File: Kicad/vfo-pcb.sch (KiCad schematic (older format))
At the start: 83 parts, among them J1 Rotery Encoder1, J10 Link-out 1-2, J11 Link-out 1-0, J12 Link-out 2-0, J13 Link-out 2-2, J14 Link-out 2-1, J15 Link-out 1-1, J2 Rotery Encoder2, J3 Analog in 3-6, J4 RxTx, J5 V12, J6 ESP32L, J7 ESP32R, J8 ILI9341, J9 Conn_01x07_Female, Q1 BFR92, Q2 BFR92, Q3 BFR92, Q4 BFR92, Q5 BFR92, Q6 BFR92, SW1 Rotary_Encoder_Switch, U1 AMS1117, U2 L7805, U3 Si5351A-B-GT, U4 Si5351A-B-GT, Y1 Crystal, Y2 Crystal

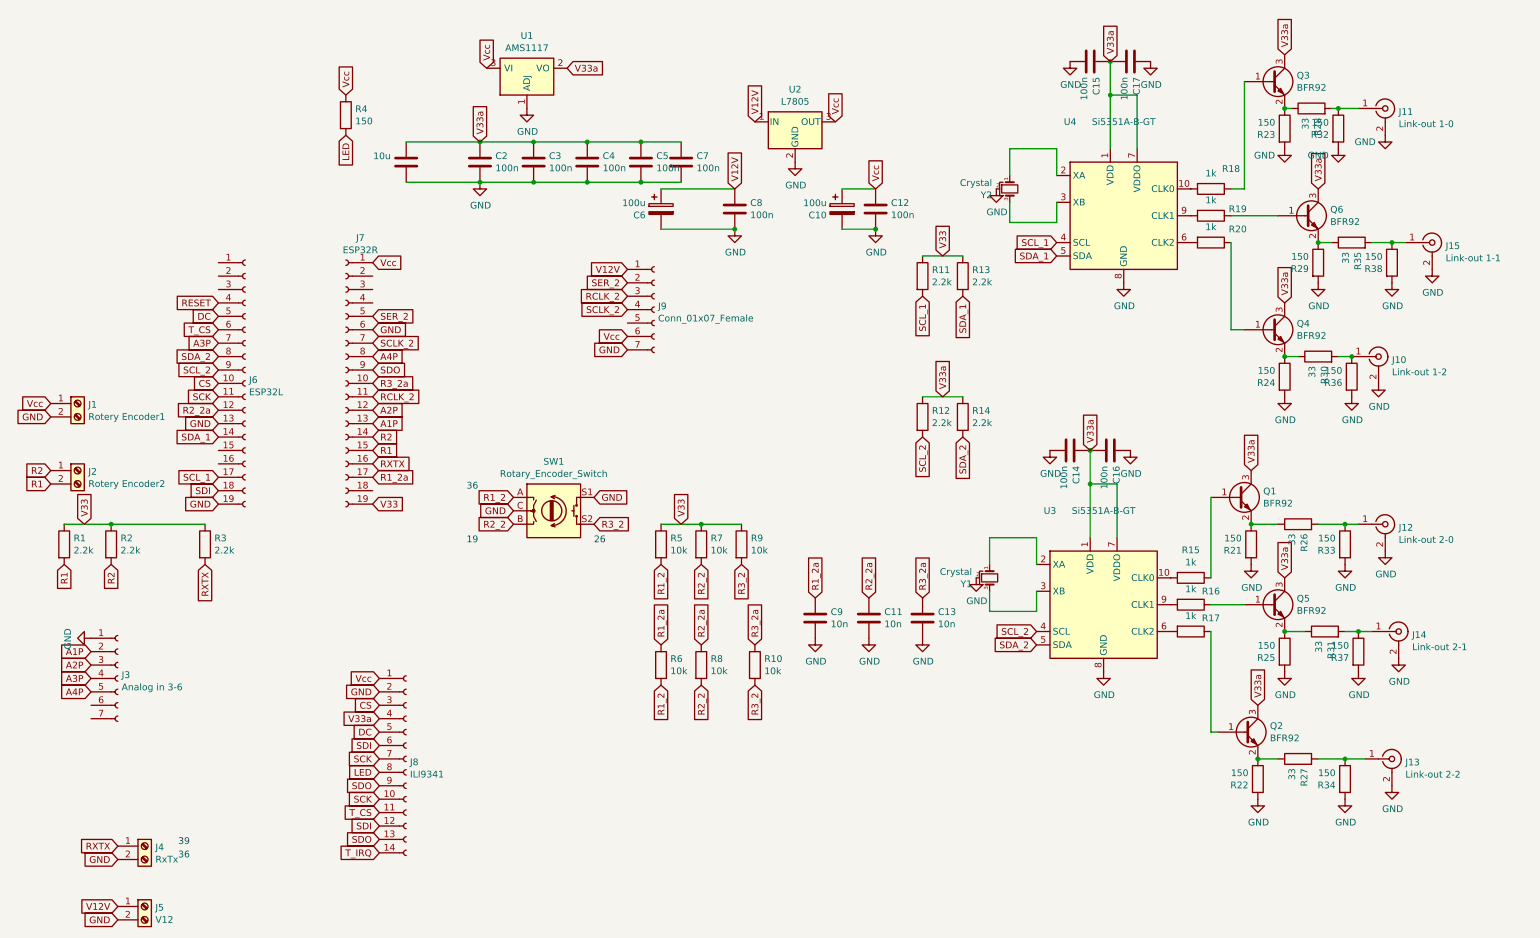
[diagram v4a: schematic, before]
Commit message: wifi update LM7805 version
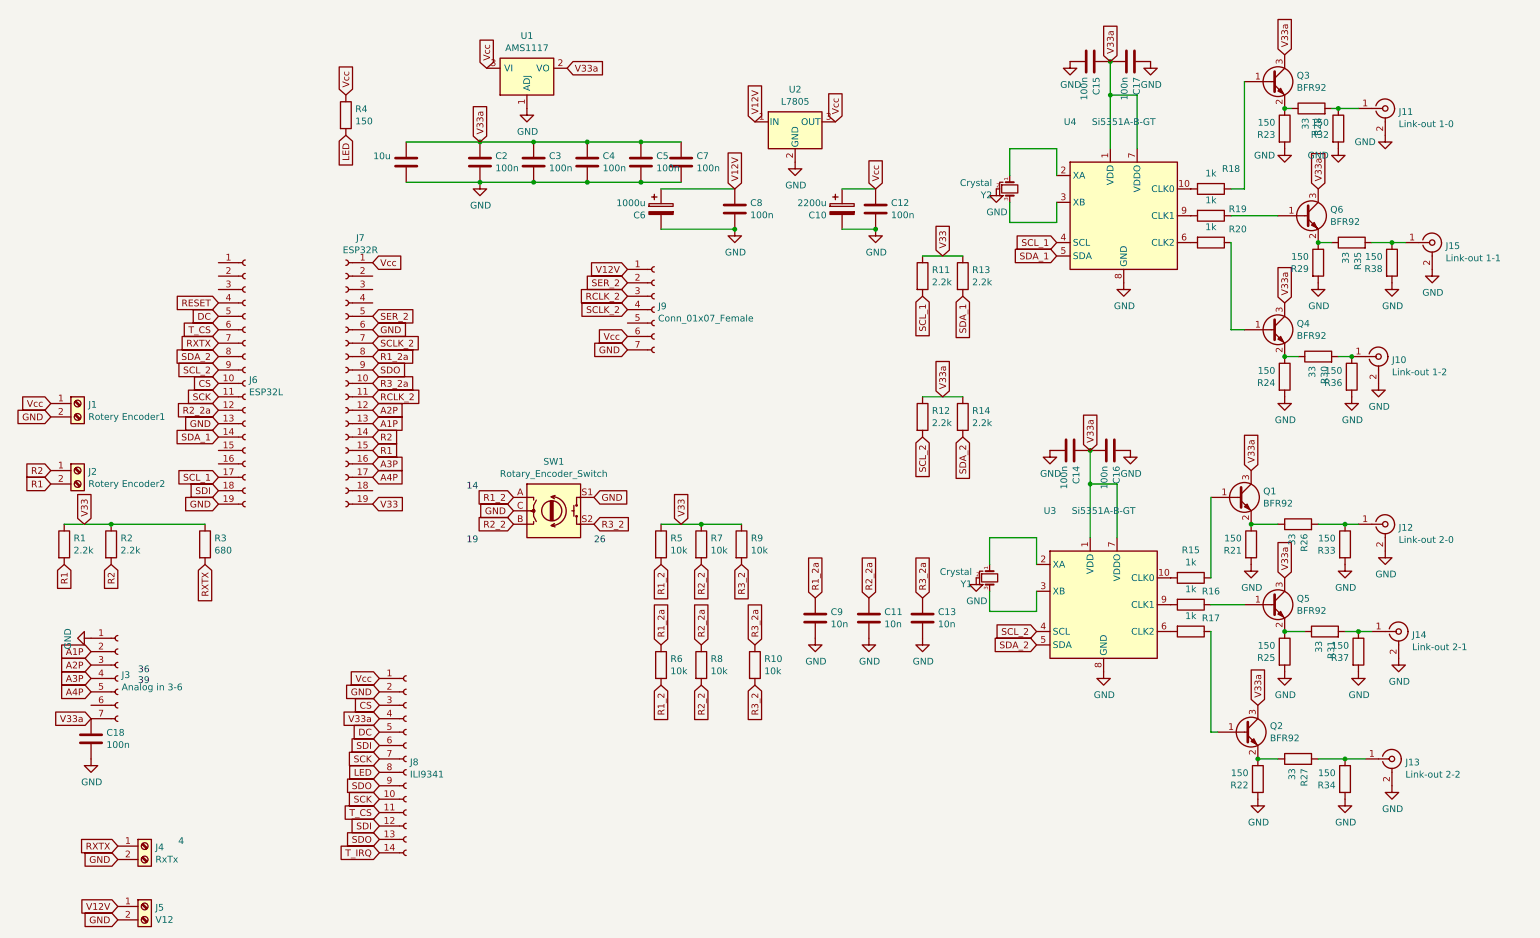
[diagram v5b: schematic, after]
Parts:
- added C18: 100n, Capacitor_SMD:C_1206_3216Metric_Pad1.42x1.75mm_HandSolder, symbol Device:C
- C10: value 100u -> 2200u; footprint Capacitor_THT:CP_Radial_D8.0mm_P3.50mm -> Capacitor_THT:CP_Radial_D10.0mm_P5.00mm
- C6: value 100u -> 1000u; footprint Capacitor_THT:CP_Radial_D8.0mm_P3.50mm -> Capacitor_THT:CP_Radial_D10.0mm_P5.00mm
- R3: value 2.2k -> 680
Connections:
- net A3P: now also J7.16 (Pin_16); no longer J6.7 (Pin_7)
- net A4P: now also J7.17 (Pin_17); no longer J7.8 (Pin_8)
- net GND: now also C18.1
- net R1_2a: now also J7.8 (Pin_8); no longer J7.17 (Pin_17)
- net RXTX: now also J6.7 (Pin_7); no longer J7.16 (Pin_16)
- net V33a: now also J3.7 (Pin_7), C18.2
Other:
- note added: "14"
- note added: "36\n39"
- note added: "4"
- note removed: "36"
- note removed: "39"
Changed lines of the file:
@@
 Text GLabel 4250 4250 0    50   Input ~ 0
 R2_2
-Text GLabel 3200 3900 2    50   Input ~ 0
+Text GLabel 3200 3000 2    50   Input ~ 0
 R1_2a
 Text GLabel 4850 4250 2    50   Input ~ 0
@@
 P 5350 1900
 F 0 "C6" H 5235 1854 50  0000 R CNN
-F 1 "100u" H 5235 1945 50  0000 R CNN
-F 2 "Capacitor_THT:CP_Radial_D8.0mm_P3.50mm" H 5388 1750 50  0001 C CNN
+F 1 "1000u" H 5235 1945 50  0000 R CNN
+F 2 "Capacitor_THT:CP_Radial_D10.0mm_P5.00mm" H 5388 1750 50  0001 C CNN
 F 3 "~" H 5350 1900 50  0001 C CNN
 	1    5350 1900
@@
 P 6700 1900
 F 0 "C10" H 6585 1854 50  0000 R CNN
-F 1 "100u" H 6585 1945 50  0000 R CNN
-F 2 "Capacitor_THT:CP_Radial_D8.0mm_P3.50mm" H 6738 1750 50  0001 C CNN
+F 1 "2200u" H 6585 1945 50  0000 R CNN
+F 2 "Capacitor_THT:CP_Radial_D10.0mm_P5.00mm" H 6738 1750 50  0001 C CNN
 F 3 "~" H 6700 1900 50  0001 C CNN
 	1    6700 1900
 	1    0    0    -1
 $EndComp
-Wire Wire Line
-	6700 1750 6950 1750
 Wire Wire Line
 	6700 2050 6950 2050
@@
 P 1950 4400
 F 0 "R3" H 2020 4446 50  0000 L CNN
-F 1 "2.2k" H 2020 4355 50  0000 L CNN
+F 1 "680" H 2020 4355 50  0000 L CNN
 F 2 "Resistor_SMD:R_1206_3216Metric_Pad1.42x1.75mm_HandSolder" V 1880 4400 50  0001 C CNN
 F 3 "~" H 1950 4400 50  0001 C CNN
@@
 R3_2a
 $Comp
-L power:GND #PWR09
-U 1 1 5D989F63
-P 7300 5100
-F 0 "#PWR09" H 7300 4850 50  0001 C CNN
-F 1 "GND" H 7305 4927 50  0000 C CNN
-F 2 "" H 7300 5100 50  0001 C CNN
-F 3 "" H 7300 5100 50  0001 C CNN
-	1    7300 5100
-	1    0    0    -1
-$EndComp
-$Comp
 L power:GND #PWR07
 U 1 1 5D98A28F
@@
 Text GLabel 6500 4800 1    50   Input ~ 0
 R1_2a
-Text GLabel 2050 2900 0    50   Input ~ 0
-A3P
-Text GLabel 3200 3000 2    50   Input ~ 0
+Text GLabel 3200 3900 2    50   Input ~ 0
 A4P
 $Comp
@@
 	0    1    1    0
 $EndComp
-Text GLabel 3200 3800 2    50   Input ~ 0
+Text GLabel 2050 2900 0    50   Input ~ 0
 RXTX
 Text GLabel 3200 3700 2    50   Input ~ 0
@@
 Text Notes 4850 4400 0    50   ~ 0
 26
-Text Notes 1750 6650 0    50   ~ 0
-39
-Text Notes 1750 6750 0    50   ~ 0
-36
 Text GLabel 1100 5200 0    50   Input ~ 0
 A1P
@@
 R2_2a
 Text Notes 3900 4000 0    50   ~ 0
-36
+14
 $Comp
 L Oscillator:Si5351A-B-GT U4
@@
 Connection ~ 10400 1150
 Connection ~ 10000 5050
+Text GLabel 1100 5700 0    50   Input ~ 0
+V33a
+$Comp
+L Device:C C18
+U 1 1 5F8B6A6A
+P 1100 5850
+F 0 "C18" H 985 5804 50  0000 R CNN
+F 1 "100n" H 985 5895 50  0000 R CNN
+F 2 "Capacitor_SMD:C_1206_3216Metric_Pad1.42x1.75mm_HandSolder" H 1138 5700 50  0001 C CNN
+F 3 "~" H 1100 5850 50  0001 C CNN
+	1    1100 5850
+	-1   0    0    1
+$EndComp
+$Comp
+L power:GND #PWR09
+U 1 1 5D989F63
+P 7300 5100
+F 0 "#PWR09" H 7300 4850 50  0001 C CNN
+F 1 "GND" H 7305 4927 50  0000 C CNN
+F 2 "" H 7300 5100 50  0001 C CNN
+F 3 "" H 7300 5100 50  0001 C CNN
+	1    7300 5100
+	1    0    0    -1
+$EndComp
+$Comp
+L power:GND #PWR036
+U 1 1 5F8B99F4
+P 1100 6000
+F 0 "#PWR036" H 1100 5750 50  0001 C CNN
+F 1 "GND" H 1105 5827 50  0000 C CNN
+F 2 "" H 1100 6000 50  0001 C CNN
+F 3 "" H 1100 6000 50  0001 C CNN
+	1    1100 6000
+	1    0    0    -1
+$EndComp
+Text Notes 1750 6650 0    50   ~ 0
+4
+Text GLabel 3200 3800 2    50   Input ~ 0
+A3P
+Text Notes 1450 5450 0    50   ~ 0
+36\n39
+Wire Wire Line
+	6700 1750 6950 1750
 $EndSCHEMATC

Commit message: change debounce
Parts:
- C11, C13, C9: value 10n -> 100n
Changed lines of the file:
@@
 P 6500 4950
 F 0 "C9" H 6385 4904 50  0000 R CNN
-F 1 "10n" H 6385 4995 50  0000 R CNN
+F 1 "100n" H 6385 4995 50  0000 R CNN
 F 2 "Capacitor_SMD:C_1206_3216Metric_Pad1.42x1.75mm_HandSolder" H 6538 4800 50  0001 C CNN
 F 3 "~" H 6500 4950 50  0001 C CNN
@@
 P 6900 4950
 F 0 "C11" H 6785 4904 50  0000 R CNN
-F 1 "10n" H 6785 4995 50  0000 R CNN
+F 1 "100n" H 6785 4995 50  0000 R CNN
 F 2 "Capacitor_SMD:C_1206_3216Metric_Pad1.42x1.75mm_HandSolder" H 6938 4800 50  0001 C CNN
 F 3 "~" H 6900 4950 50  0001 C CNN
@@
 P 7300 4950
 F 0 "C13" H 7185 4904 50  0000 R CNN
-F 1 "10n" H 7185 4995 50  0000 R CNN
+F 1 "100n" H 7185 4995 50  0000 R CNN
 F 2 "Capacitor_SMD:C_1206_3216Metric_Pad1.42x1.75mm_HandSolder" H 7338 4800 50  0001 C CNN
 F 3 "~" H 7300 4950 50  0001 C CNN
